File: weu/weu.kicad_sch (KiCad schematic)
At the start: 0 parts

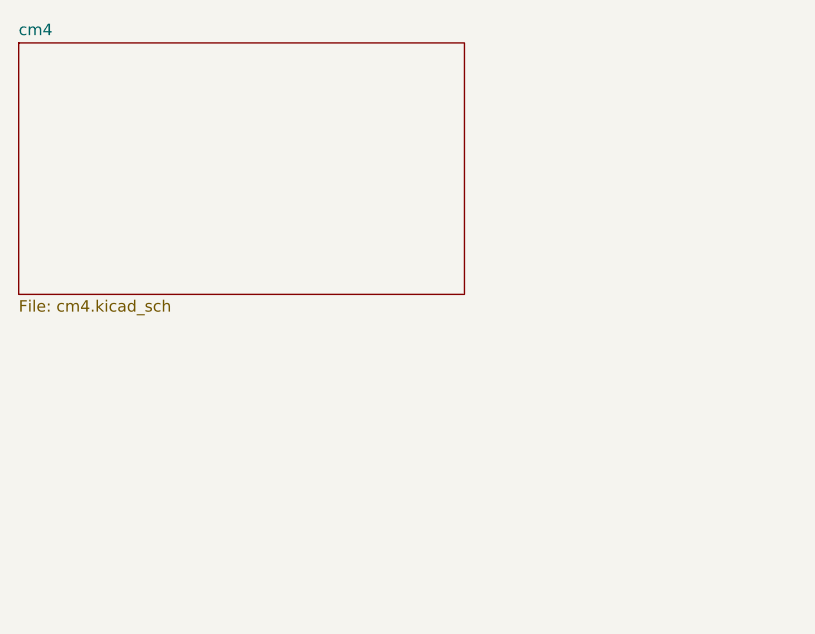
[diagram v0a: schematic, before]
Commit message: Added usb hub ic and esp32
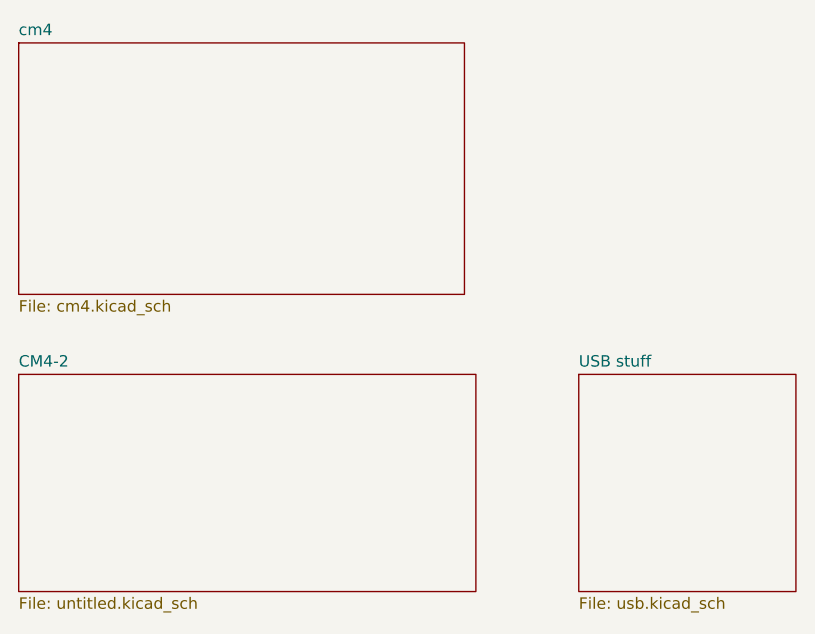
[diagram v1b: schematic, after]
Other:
- added sheet CM4-2 (untitled.kicad_sch)
- added sheet USB stuff (usb.kicad_sch)
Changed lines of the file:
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@@
+		)
+	)
+	(sheet
+		(at 176.53 110.49)
+		(size 24.13 24.13)
+		(exclude_from_sim no)
+		(in_bom yes)
+		(on_board yes)
+		(dnp no)
+		(fields_autoplaced yes)
+		(stroke
+			(width 0.1524)
+			(type solid)
+		)
+		(fill
+			(color 0 0 0 0.0000)
+		)
+		(property "Sheetname" "USB stuff"
+			(at 176.53 109.7784 0)
+			(effects
+				(font
+					(size 1.27 1.27)
+				)
+				(justify left bottom)
+			)
+		)
+		(property "Sheetfile" "usb.kicad_sch"
+			(at 176.53 135.2046 0)
+			(effects
+				(font
+					(size 1.27 1.27)
+				)
+				(justify left top)
+			)
+		)
+		(instances
+			(project "weu"
+				(path "/dcbea2a6-438c-4c89-8cc5-bc5cbeb8189c"
+					(page "4")
+				)
+			)
+		)
+	)
+	(sheet
+		(at 114.3 110.49)
+		(size 50.8 24.13)
+		(exclude_from_sim no)
+		(in_bom yes)
+		(on_board yes)
+		(dnp no)
+		(fields_autoplaced yes)
+		(stroke
+			(width 0.1524)
+			(type solid)
+		)
+		(fill
+			(color 0 0 0 0.0000)
+		)
+		(property "Sheetname" "CM4-2"
+			(at 114.3 109.7784 0)
+			(effects
+				(font
+					(size 1.27 1.27)
+				)
+				(justify left bottom)
+			)
+		)
+		(property "Sheetfile" "untitled.kicad_sch"
+			(at 114.3 135.2046 0)
+			(effects
+				(font
+					(size 1.27 1.27)
+				)
+				(justify left top)
+			)
+		)
+		(instances
+			(project "weu"
+				(path "/dcbea2a6-438c-4c89-8cc5-bc5cbeb8189c"
+					(page "3")
+				)
+			)
 		)
 	)
